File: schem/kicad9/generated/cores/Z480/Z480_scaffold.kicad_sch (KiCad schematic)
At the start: 0 parts

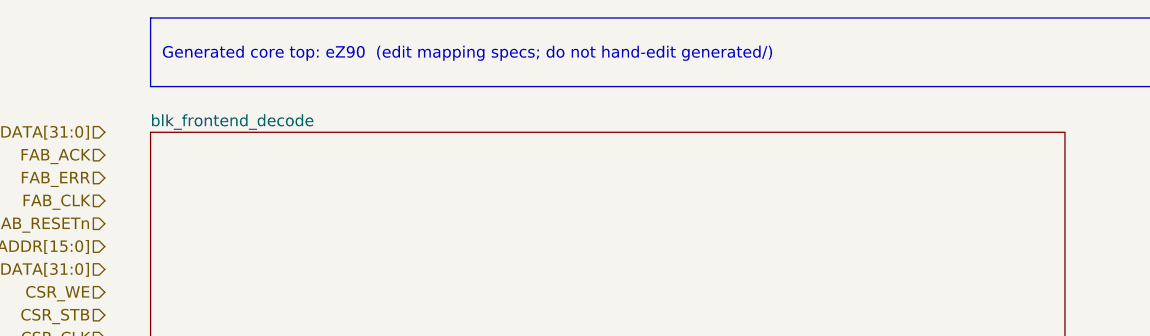
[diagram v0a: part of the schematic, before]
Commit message: systems: rename CarbonEZ90 to CarbonZ480 and refresh maps
Detailed description:
- What changed: renamed the CarbonEZ90 system to CarbonZ480, updated system tops for Z480 tier IDs and boot signatures, refreshed memory map docs and carbon_memmap_pkg, and updated KiCad kicadgen specs plus regenerated Z480/CarbonZ480 schematics.
- Why it changed: keep system naming, maps, and schematics consistent with the new Z480 tier model.
- Files/paths affected: hdl/systems/CarbonZ480/*, hdl/systems/CarbonEZ90/* (removed), hdl/systems/CarbonZ80/*, hdl/systems/CarbonZ90/*, hdl/systems/CarbonX86/*, hdl/systems/CarbonX96/*, hdl/systems/common/rtl/carbon_memmap_pkg.sv, schem/kicad9/spec/kicadgen_*.yaml, schem/kicad9/generated/cores/Z480, schem/kicad9/generated/systems/CarbonZ480.
- Any compatibility notes: reset still enters P0; Z480 presents as P7; memory map ranges stay stable aside from naming.
- What remains TODO: update sim harnesses and documentation references to the new names.
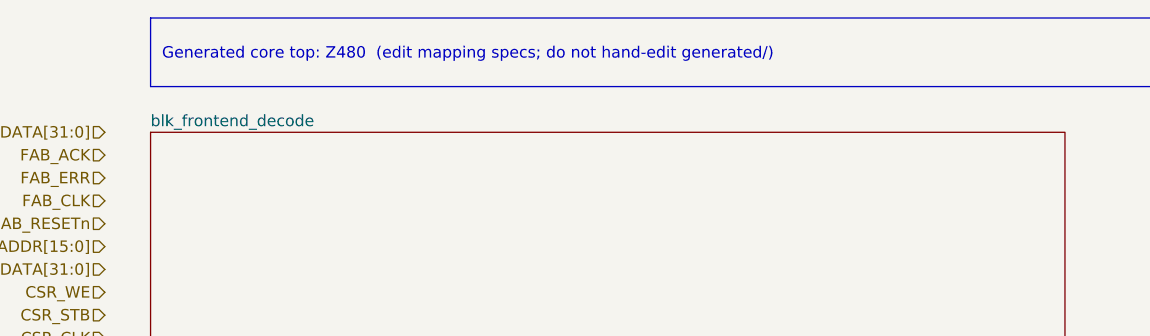
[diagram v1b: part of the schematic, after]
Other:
- title: eZ90 (generated) -> Z480 (generated)
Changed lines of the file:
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@@
 	(paper "A3")
 	(title_block
-		(title "eZ90 (generated)")
+		(title "Z480 (generated)")
 		(company "Project Carbon")
 		(comment 1 "Generated - do not edit in generated/")
@@
 	)
 	(text_box
-		"Generated core top: eZ90  (edit mapping specs; do not hand-edit generated/)"
+		"Generated core top: Z480  (edit mapping specs; do not hand-edit generated/)"
 		(exclude_from_sim no)
 		(at
@@
 		(instances
 			(project
-				"core_eZ90"
+				"core_Z480"
 				(path
 					"/59d3f377-8086-5e08-87f2-a6ea56e5a5df"
@@
 		(instances
 			(project
-				"core_eZ90"
+				"core_Z480"
 				(path
 					"/59d3f377-8086-5e08-87f2-a6ea56e5a5df"
@@
 		(instances
 			(project
-				"core_eZ90"
+				"core_Z480"
 				(path
 					"/59d3f377-8086-5e08-87f2-a6ea56e5a5df"
@@
 		(instances
 			(project
-				"core_eZ90"
+				"core_Z480"
 				(path
 					"/59d3f377-8086-5e08-87f2-a6ea56e5a5df"
@@
 		(instances
 			(project
-				"core_eZ90"
-				(path
-					"/59d3f377-8086-5e08-87f2-a6ea56e5a5df"
+				"core_Z480"
+				(path
+					"/59d3f377-8086-5e08-87f2-a6ea56e5a5df"
